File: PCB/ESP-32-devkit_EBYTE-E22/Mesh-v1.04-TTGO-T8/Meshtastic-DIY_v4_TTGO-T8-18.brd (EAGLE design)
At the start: 72.4 x 38.1 mm, 20 parts

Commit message: [PCB] Fixed `v1.04-TTGO-T8` & description update (#12)
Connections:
- removed net 12: J2.3, TTGO-T8_V1.8.12
- new net 14: J2.3, TTGO-T8_V1.8.14
- net RXEN: now also TTGO-T8_V1.8.12; no longer TTGO-T8_V1.8.14
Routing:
- net 12: track 18.8 -> 0.00 mm
- net 14: track 0.00 -> 17.9 mm
- net 26: track 23.3 -> 20.0 mm
- net RXEN: track 19.8 -> 22.3 mm
- net VP: track 28.7 -> 27.6 mm
- net 35: track 26.1 -> 25.1 mm
- net 34: track 25.9 -> 25.1 mm
- net 25: track 20.7 -> 20.0 mm
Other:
- board text added: "14"
- board text removed: "12"

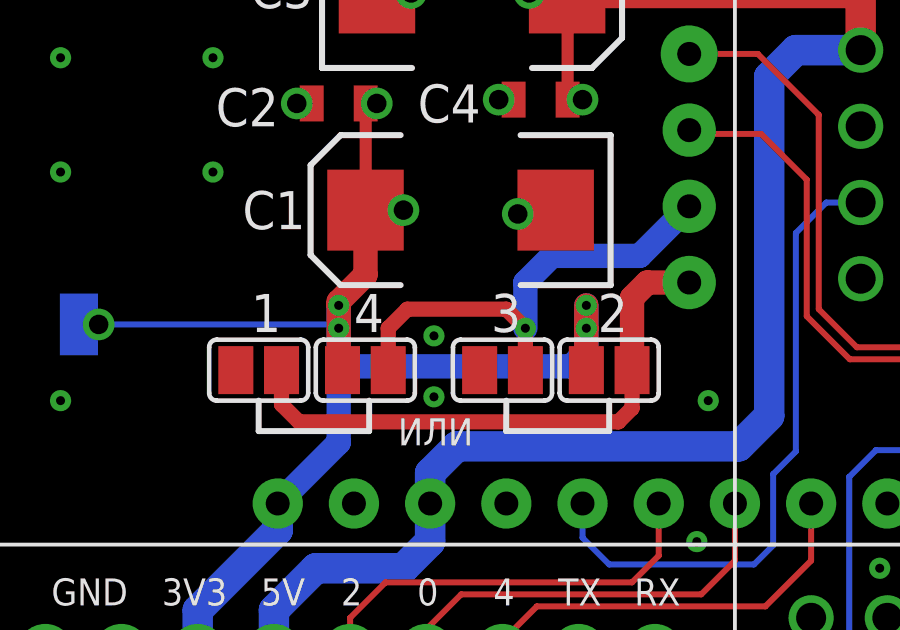
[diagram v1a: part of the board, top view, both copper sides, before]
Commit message: PCB updates (#15)
* fixes PCB version and description

* Updated revision of the v1.01 PCB

* Fixed drill layout for v.1.05

* Updated EBYTE E22 adapter (removed excessive antenna line)

* Updated PCB v1.03

* Updated PCB v1.02

* Removed untested PCB design

* [PCB] Missing brd&sch for 1.01 & updated 1.02

* v1.04 update

* [PCB] Meshtastic-DIY_v1.06 - TTGO T-Energy T18 V3.0 HAT
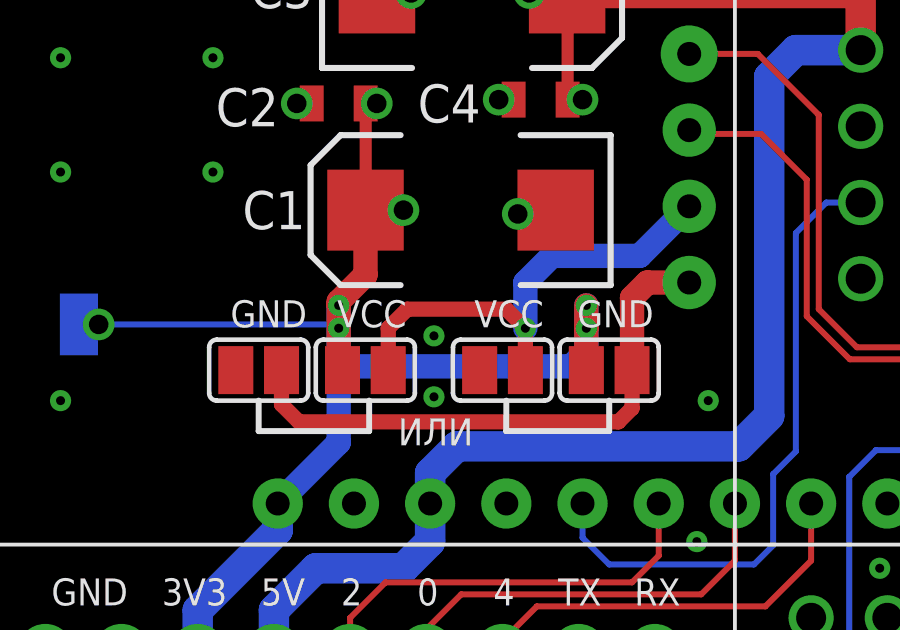
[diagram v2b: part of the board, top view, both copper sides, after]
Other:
- board text added: "VCC"
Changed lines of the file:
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@@
 <drawing>
 <settings>
-<setting alwaysvectorfont="no"/>
+<setting alwaysvectorfont="yes"/>
 <setting verticaltext="up"/>
 </settings>
@@
 <text x="33.985" y="27.083" size="0.9" layer="25" font="vector" ratio="18">М22</text>
 <wire x1="37.719" y1="27.432" x2="38.608" y2="27.432" width="0.2" layer="25"/>
+<text x="14.554" y="13.875" size="0.9" layer="25" font="vector" ratio="18">GND</text>
+<text x="18.11" y="13.875" size="0.9" layer="25" font="vector" ratio="18">VCC</text>
+<text x="22.682" y="13.875" size="0.9" layer="25" font="vector" ratio="18">VCC</text>
+<text x="26.111" y="13.875" size="0.9" layer="25" font="vector" ratio="18">GND</text>
 </plain>
 <attributes>
@@
 </element>
 <element name="1" library="jumper" library_urn="urn:adsk.eagle:library:252" package="SJ" package3d_urn="urn:adsk.eagle:package:15471/1" value="" x="15.494" y="12.446" smashed="yes">
-<attribute name="NAME" x="15.24" y="13.716" size="1.27" layer="25" ratio="10"/>
 <attribute name="POPULARITY" value="33" x="15.494" y="12.446" size="1.778" layer="27" display="off"/>
 <attribute name="VALUE" x="15.8941" y="12.446" size="0.02" layer="27"/>
 </element>
 <element name="2" library="jumper" library_urn="urn:adsk.eagle:library:252" package="SJ" package3d_urn="urn:adsk.eagle:package:15471/1" value="" x="27.178" y="12.446" smashed="yes">
-<attribute name="NAME" x="26.797" y="13.716" size="1.27" layer="25" ratio="10"/>
 <attribute name="POPULARITY" value="33" x="23.241" y="8.382" size="1.778" layer="27" display="off"/>
 <attribute name="VALUE" x="27.5781" y="12.446" size="0.02" layer="27"/>
 </element>
 <element name="3" library="jumper" library_urn="urn:adsk.eagle:library:252" package="SJ" package3d_urn="urn:adsk.eagle:package:15471/1" value="" x="23.622" y="12.446" smashed="yes">
-<attribute name="NAME" x="23.241" y="13.716" size="1.27" layer="25" ratio="10"/>
 <attribute name="POPULARITY" value="33" x="23.622" y="8.382" size="1.778" layer="27" display="off"/>
 <attribute name="VALUE" x="24.0221" y="12.446" size="0.02" layer="27"/>
 </element>
 <element name="4" library="jumper" library_urn="urn:adsk.eagle:library:252" package="SJ" package3d_urn="urn:adsk.eagle:package:15471/1" value="" x="19.05" y="12.446" smashed="yes">
-<attribute name="NAME" x="18.669" y="13.716" size="1.27" layer="25" ratio="10"/>
 <attribute name="POPULARITY" value="33" x="15.113" y="4.318" size="1.778" layer="27" display="off"/>
 <attribute name="VALUE" x="19.4501" y="12.446" size="0.02" layer="27"/>
